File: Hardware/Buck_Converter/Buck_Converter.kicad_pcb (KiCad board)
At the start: 2 copper layers, 14.6 x 13 mm, 17 parts, among them J1 Conn_01x05, U1 AP62200WU, U2 AP62200WU

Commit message: Reviewed
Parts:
- J1: moved to F.Cu
- turned J1 to 0 degrees
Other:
- board size 14.6 x 13 mm -> 14.7 x 13 mm

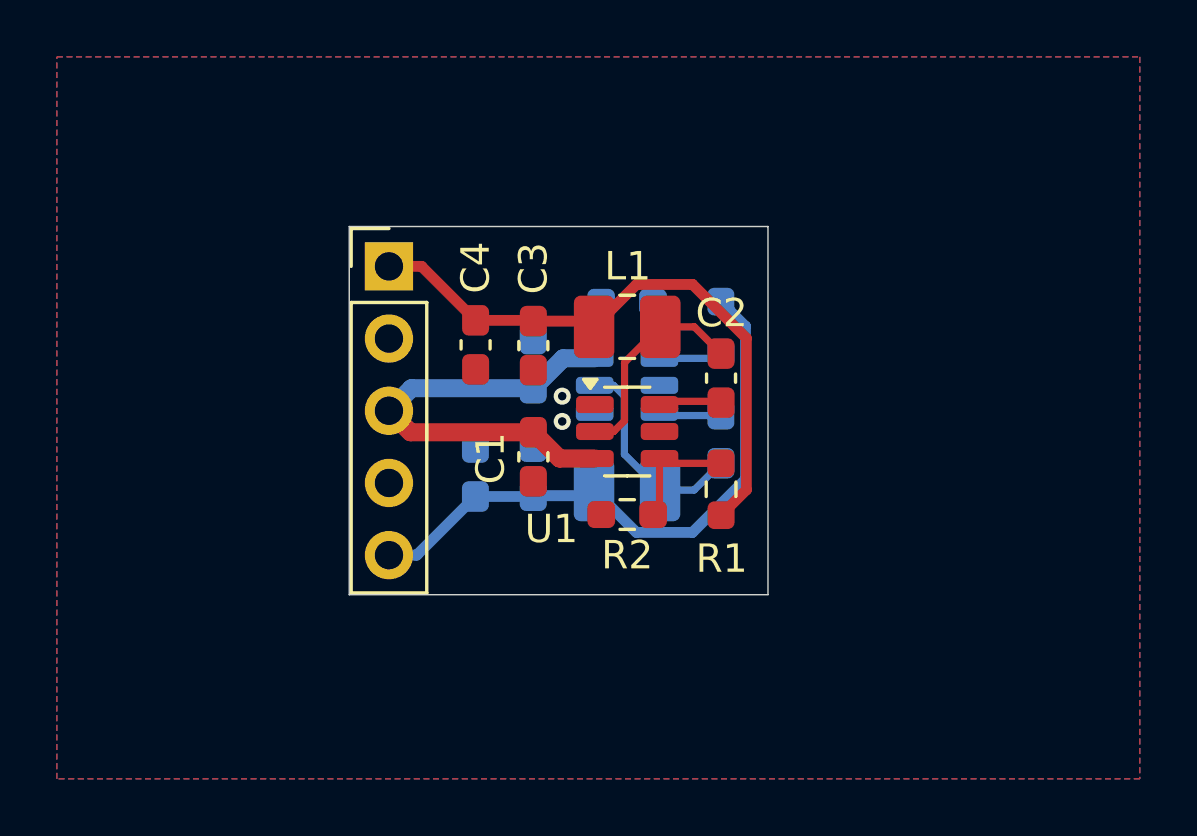
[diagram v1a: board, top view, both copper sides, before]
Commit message: Add Buck Converter pin labels
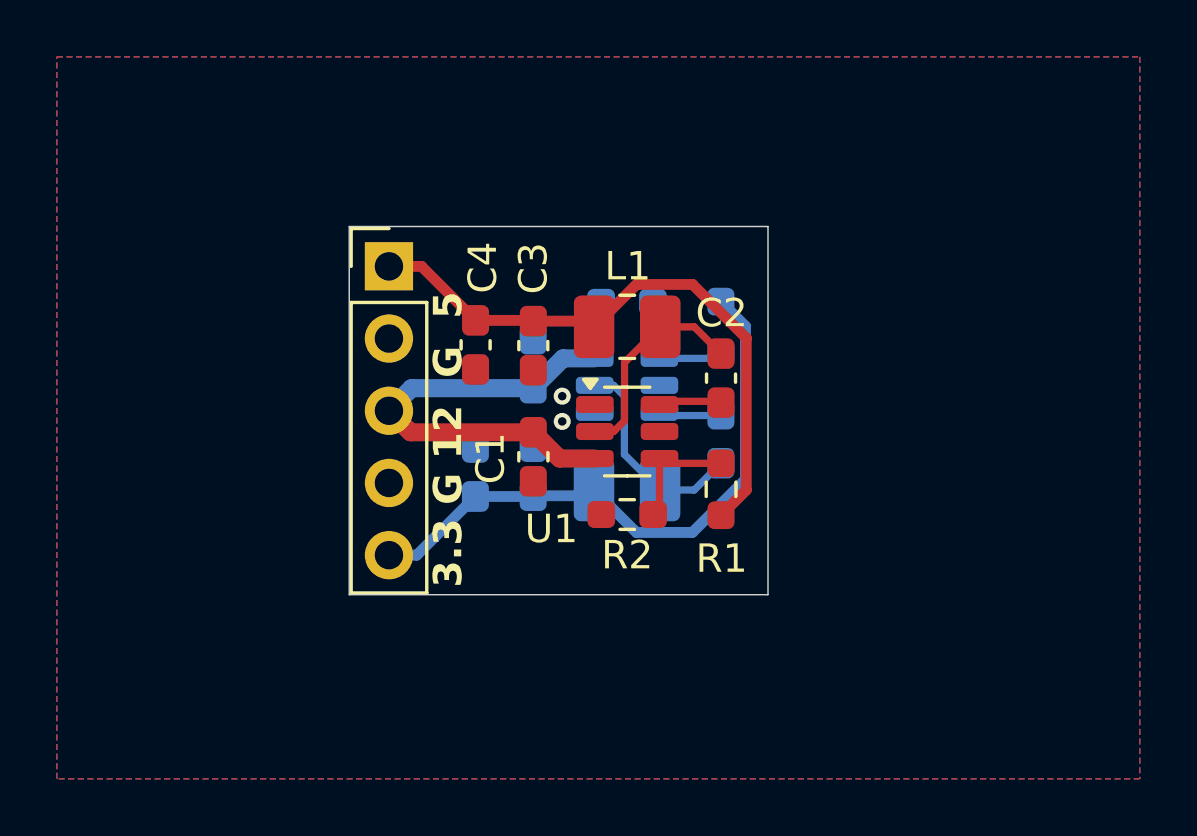
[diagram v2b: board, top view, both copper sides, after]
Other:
- board text added: "3.3 G 12 G 5"
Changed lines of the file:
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@@
 		(tags "capacitor handsolder")
 		(property "Reference" "C4"
-			(at -2.72 0 90)
+			(at -2.72 -0.254 90)
 			(layer "F.SilkS")
 			(effects
@@
 		(tags "capacitor handsolder")
 		(property "Reference" "C8"
-			(at -2.7675 0 90)
+			(at -2.7675 0.2595 90)
 			(layer "B.SilkS")
 			(effects
@@
 		(layer "Edge.Cuts")
 	)
+	(gr_text "3.3 G 12  G  5"
+		(at 140.081 82.169 -90)
+		(layer "B.SilkS")
+		(effects
+			(font
+				(size 1 1)
+				(thickness 0.2)
+				(bold yes)
+			)
+			(justify left bottom mirror)
+		)
+	)
+	(gr_text "3.3 G 12  G  5"
+		(at 141.351 82.169 90)
+		(layer "F.SilkS")
+		(effects
+			(font
+				(size 1 1)
+				(thickness 0.2)
+				(bold yes)
+			)
+			(justify left bottom)
+		)
+	)
 	(via

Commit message: Prepare for board review
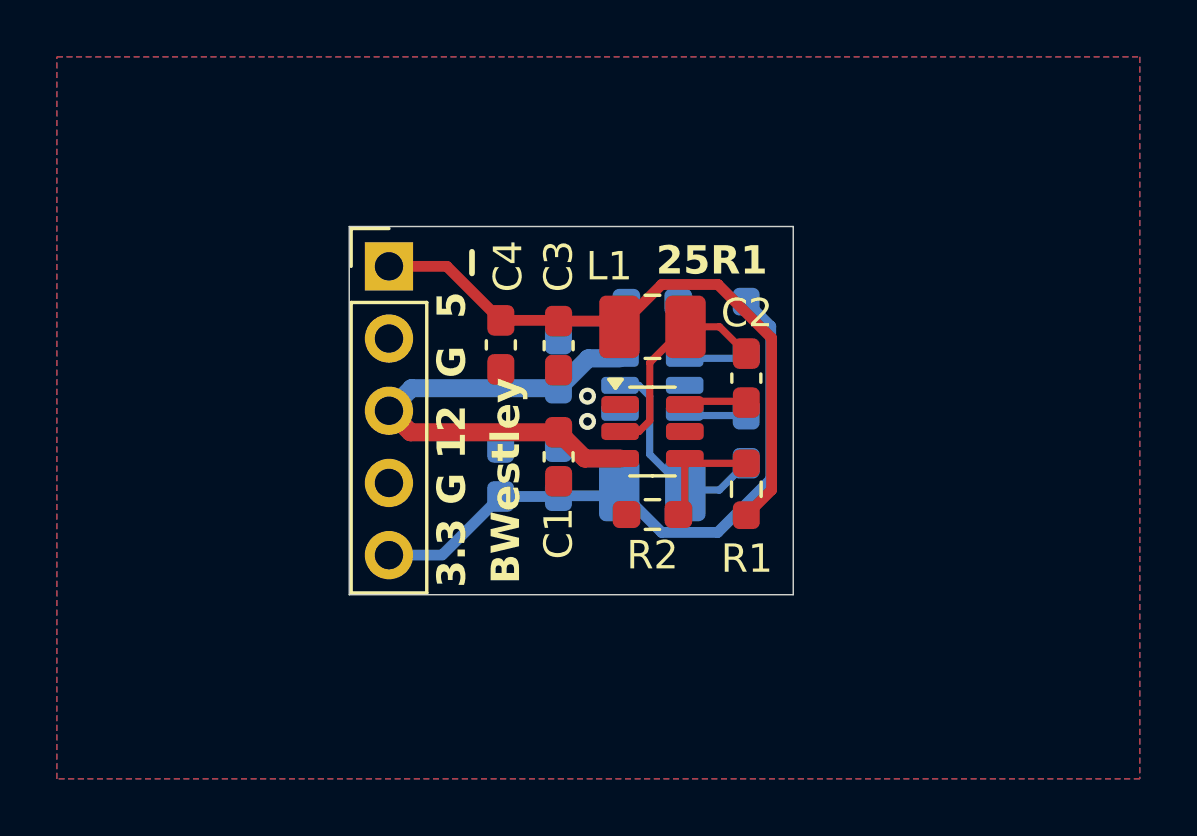
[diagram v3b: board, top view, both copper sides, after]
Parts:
- moved C2 0.89 mm to (151.3, 74.8)
- moved C4 0.89 mm to (142.6, 73.6)
- moved C5 0.89 mm to (144.6, 74.3)
- moved C7 0.89 mm to (144.6, 78.1)
- moved C8 0.89 mm to (142.6, 78.1)
- moved L1 0.89 mm to (148.0, 73.0)
- moved L2 0.89 mm to (147.9, 78.7)
- moved R1 0.89 mm to (151.3, 78.7)
- moved R2 0.89 mm to (148.0, 79.6)
- moved R4 0.89 mm to (147.9, 72.1)
- moved U1 0.89 mm to (148.0, 76.7)
- moved U2 0.89 mm to (147.9, 75.1)
- moved C1 0.89 mm to (144.7, 77.6)
- moved C3 0.89 mm to (144.7, 73.7)
- moved C6 0.89 mm to (151.3, 76.9)
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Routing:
- net +12V: track 15.9 -> 17.7 mm
- net +5V: track 21.1 -> 22.0 mm
- net +3V3: track 21.2 -> 22.0 mm
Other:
- board size 14.7 x 13 mm -> 15.6 x 13 mm
- board text added: "25R1"
- board text added: "5 G 12 G 3.3"
- board text added: "BWestley"
- board text added: "MEhlers"
